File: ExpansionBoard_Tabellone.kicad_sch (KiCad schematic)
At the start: 20 parts, among them J101 RELAY, J102 UART, J103 I2C, J104 Conn_01x15, J105 Conn_01x15, J106 5V, J107 GND, J108 3V3, J109 GPIO, J110 LED, J111 RESET, J112 I2C, J113 RTC, J114 I2C

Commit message: Modificato footprint TabelloneBoard
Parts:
- U102: footprint MCU_Espressif_Footprints:ESP_WROOM_32_DevKit_HandSoldering -> PersonalLibrary:TabelloneBoard_HandSoldering
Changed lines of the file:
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@@
       (effects (font (size 1.27 1.27)))
     )
-    (property "Footprint" "MCU_Espressif_Footprints:ESP_WROOM_32_DevKit_HandSoldering" (at 105.41 27.94 0)
+    (property "Footprint" "PersonalLibrary:TabelloneBoard_HandSoldering" (at 105.41 27.94 0)
       (effects (font (size 1.27 1.27)) hide)
     )
@@
       (effects (font (size 1.27 1.27)))
     )
-    (property "Footprint" "MCU_Espressif_Footprints:ESP_WROOM_32_DevKit_HandSoldering" (at 31.75 27.94 0)
+    (property "Footprint" "PersonalLibrary:TabelloneBoard_HandSoldering" (at 31.75 27.94 0)
       (effects (font (size 1.27 1.27)) hide)
     )

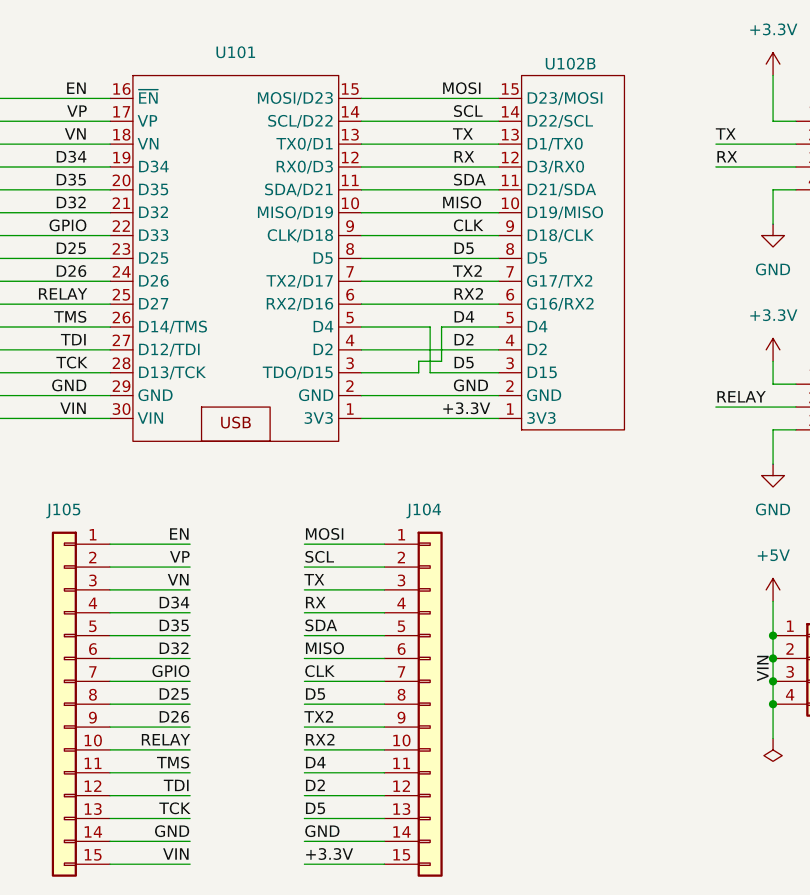
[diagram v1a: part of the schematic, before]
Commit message: Spostate le label lato Pin ESP e non lato board
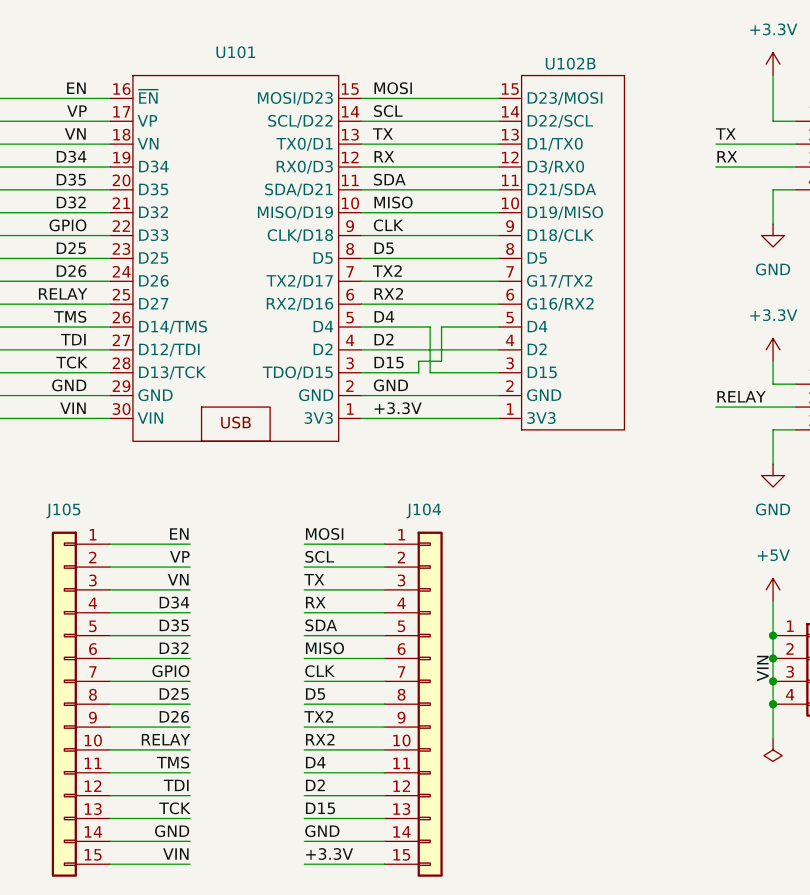
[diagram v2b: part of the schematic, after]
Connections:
- net D4: now also U101.5 (D4), U102.3 (D15); no longer U101.3 (TDO/D15), U102.5 (D4)
- net D5: no longer J104.13 (Pin_13), U101.5 (D4), U102.3 (D15)
- new net D15: J104.13 (Pin_13), U101.3 (TDO/D15), U102.5 (D4)

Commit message: Cambiate le impronte ai connettori
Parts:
- J101: footprint Connector_PinSocket_2.54mm:PinSocket_1x03_P2.54mm_Vertical -> Connector_Header_P2.54_my:PinSocket_1x03_P2.54mm_Vertical_HandSoldering
- J102, J103, J106, J107, J108, J112, J113, J114: footprint Connector_PinSocket_2.54mm:PinSocket_1x04_P2.54mm_Vertical -> Connector_Header_P2.54_my:PinSocket_1x04_P2.54mm_Vertical_HandSoldering
- J104, J105: footprint Connector_PinSocket_2.54mm:PinSocket_1x15_P2.54mm_Vertical -> Connector_Header_P2.54_my:PinSocket_1x15_P2.54mm_Vertical_HandSoldering
- J109: footprint (none) -> Connector_Header_P2.54_my:PinSocket_1x03_P2.54mm_Vertical_HandSoldering
- J110, J111: footprint (none) -> Connector_Header_P2.54_my:PinSocket_1x02_P2.54mm_Vertical_HandSoldering
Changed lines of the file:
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@@
       (effects (font (size 1.27 1.27)) (justify left))
     )
-    (property "Footprint" "Connector_PinSocket_2.54mm:PinSocket_1x04_P2.54mm_Vertical" (at 167.64 92.71 0)
+    (property "Footprint" "Connector_Header_P2.54_my:PinSocket_1x04_P2.54mm_Vertical_HandSoldering" (at 167.64 92.71 0)
       (effects (font (size 1.27 1.27)) hide)
     )
@@
       (effects (font (size 1.27 1.27)) (justify left) hide)
     )
-    (property "Footprint" "Connector_PinSocket_2.54mm:PinSocket_1x15_P2.54mm_Vertical" (at 93.98 97.79 0)
+    (property "Footprint" "Connector_Header_P2.54_my:PinSocket_1x15_P2.54mm_Vertical_HandSoldering" (at 93.98 97.79 0)
       (effects (font (size 1.27 1.27)) hide)
     )
@@
       (effects (font (size 1.27 1.27)) (justify left))
     )
-    (property "Footprint" "Connector_PinSocket_2.54mm:PinSocket_1x03_P2.54mm_Vertical" (at 139.7 64.77 0)
+    (property "Footprint" "Connector_Header_P2.54_my:PinSocket_1x03_P2.54mm_Vertical_HandSoldering" (at 139.7 64.77 0)
       (effects (font (size 1.27 1.27)) hide)
     )
@@
       (effects (font (size 1.27 1.27)) (justify left))
     )
-    (property "Footprint" "Connector_PinSocket_2.54mm:PinSocket_1x04_P2.54mm_Vertical" (at 237.49 92.71 0)
+    (property "Footprint" "Connector_Header_P2.54_my:PinSocket_1x04_P2.54mm_Vertical_HandSoldering" (at 237.49 92.71 0)
       (effects (font (size 1.27 1.27)) hide)
     )
@@
       (effects (font (size 1.27 1.27)) (justify left))
     )
-    (property "Footprint" "" (at 165.1 64.77 0)
+    (property "Footprint" "Connector_Header_P2.54_my:PinSocket_1x03_P2.54mm_Vertical_HandSoldering" (at 165.1 64.77 0)
       (effects (font (size 1.27 1.27)) hide)
     )
@@
       (effects (font (size 1.27 1.27)) (justify left))
     )
-    (property "Footprint" "Connector_PinSocket_2.54mm:PinSocket_1x04_P2.54mm_Vertical" (at 201.93 64.77 0)
+    (property "Footprint" "Connector_Header_P2.54_my:PinSocket_1x04_P2.54mm_Vertical_HandSoldering" (at 201.93 64.77 0)
       (effects (font (size 1.27 1.27)) hide)
     )
@@
       (effects (font (size 1.27 1.27)) (justify left))
     )
-    (property "Footprint" "" (at 201.93 34.29 0)
+    (property "Footprint" "Connector_Header_P2.54_my:PinSocket_1x02_P2.54mm_Vertical_HandSoldering" (at 201.93 34.29 0)
       (effects (font (size 1.27 1.27)) hide)
     )
@@
       (effects (font (size 1.27 1.27)) (justify left))
     )
-    (property "Footprint" "Connector_PinSocket_2.54mm:PinSocket_1x04_P2.54mm_Vertical" (at 139.7 35.56 0)
+    (property "Footprint" "Connector_Header_P2.54_my:PinSocket_1x04_P2.54mm_Vertical_HandSoldering" (at 139.7 35.56 0)
       (effects (font (size 1.27 1.27)) hide)
     )
@@
       (effects (font (size 1.27 1.27)) (justify left))
     )
-    (property "Footprint" "Connector_PinSocket_2.54mm:PinSocket_1x04_P2.54mm_Vertical" (at 152.4 92.71 0)
+    (property "Footprint" "Connector_Header_P2.54_my:PinSocket_1x04_P2.54mm_Vertical_HandSoldering" (at 152.4 92.71 0)
       (effects (font (size 1.27 1.27)) hide)
     )
@@
       (effects (font (size 1.27 1.27)) (justify left))
     )
-    (property "Footprint" "" (at 240.03 34.29 0)
+    (property "Footprint" "Connector_Header_P2.54_my:PinSocket_1x02_P2.54mm_Vertical_HandSoldering" (at 240.03 34.29 0)
       (effects (font (size 1.27 1.27)) hide)
     )
@@
       (effects (font (size 1.27 1.27)) hide)
     )
-    (property "Footprint" "Connector_PinSocket_2.54mm:PinSocket_1x15_P2.54mm_Vertical" (at 53.34 97.79 0)
+    (property "Footprint" "Connector_Header_P2.54_my:PinSocket_1x15_P2.54mm_Vertical_HandSoldering" (at 53.34 97.79 0)
       (effects (font (size 1.27 1.27)) hide)
     )
@@
       (effects (font (size 1.27 1.27)) (justify left))
     )
-    (property "Footprint" "Connector_PinSocket_2.54mm:PinSocket_1x04_P2.54mm_Vertical" (at 237.49 64.77 0)
+    (property "Footprint" "Connector_Header_P2.54_my:PinSocket_1x04_P2.54mm_Vertical_HandSoldering" (at 237.49 64.77 0)
       (effects (font (size 1.27 1.27)) hide)
     )
@@
       (effects (font (size 1.27 1.27)) (justify left))
     )
-    (property "Footprint" "Connector_PinSocket_2.54mm:PinSocket_1x04_P2.54mm_Vertical" (at 137.16 92.71 0)
+    (property "Footprint" "Connector_Header_P2.54_my:PinSocket_1x04_P2.54mm_Vertical_HandSoldering" (at 137.16 92.71 0)
       (effects (font (size 1.27 1.27)) hide)
     )
@@
       (effects (font (size 1.27 1.27)) (justify left))
     )
-    (property "Footprint" "Connector_PinSocket_2.54mm:PinSocket_1x04_P2.54mm_Vertical" (at 201.93 92.71 0)
-      (effects (font (size 1.27 1.27)) hide)
-    )
+    (property "Footprint" "Connector_Header_P2.54_my:PinSocket_1x04_P2.54mm_Vertical_HandSoldering" (at 201.93 92.71 0)
+      (effects (font (size 1.27 1.27)) hide)
+    )

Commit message: Cambiato un footprint
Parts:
- R101: footprint Resistor_THT:R_Axial_DIN0309_L9.0mm_D3.2mm_P15.24mm_Horizontal -> Resistor_THT:R_Axial_DIN0309_L9.0mm_D3.2mm_P12.70mm_Horizontal
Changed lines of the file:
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@@
       (effects (font (size 1.27 1.27)))
     )
-    (property "Footprint" "Resistor_THT:R_Axial_DIN0309_L9.0mm_D3.2mm_P15.24mm_Horizontal" (at 187.96 32.512 90)
+    (property "Footprint" "Resistor_THT:R_Axial_DIN0309_L9.0mm_D3.2mm_P12.70mm_Horizontal" (at 187.96 32.512 90)
       (effects (font (size 1.27 1.27)) hide)
     )

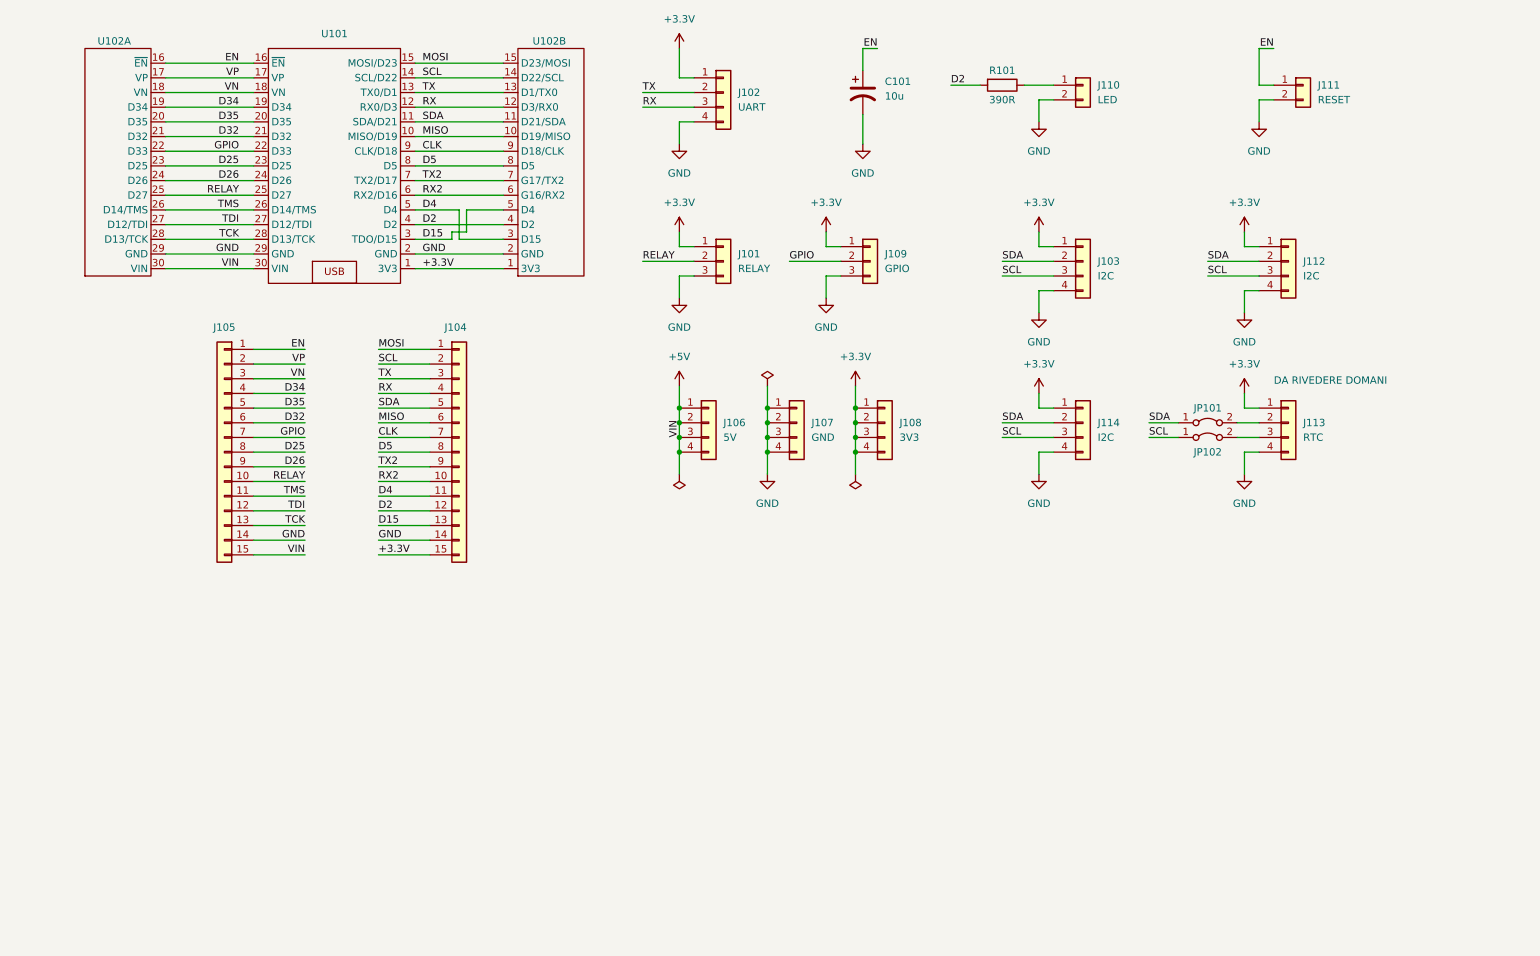
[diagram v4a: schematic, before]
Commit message: Aggiunti i Relè nello schematico
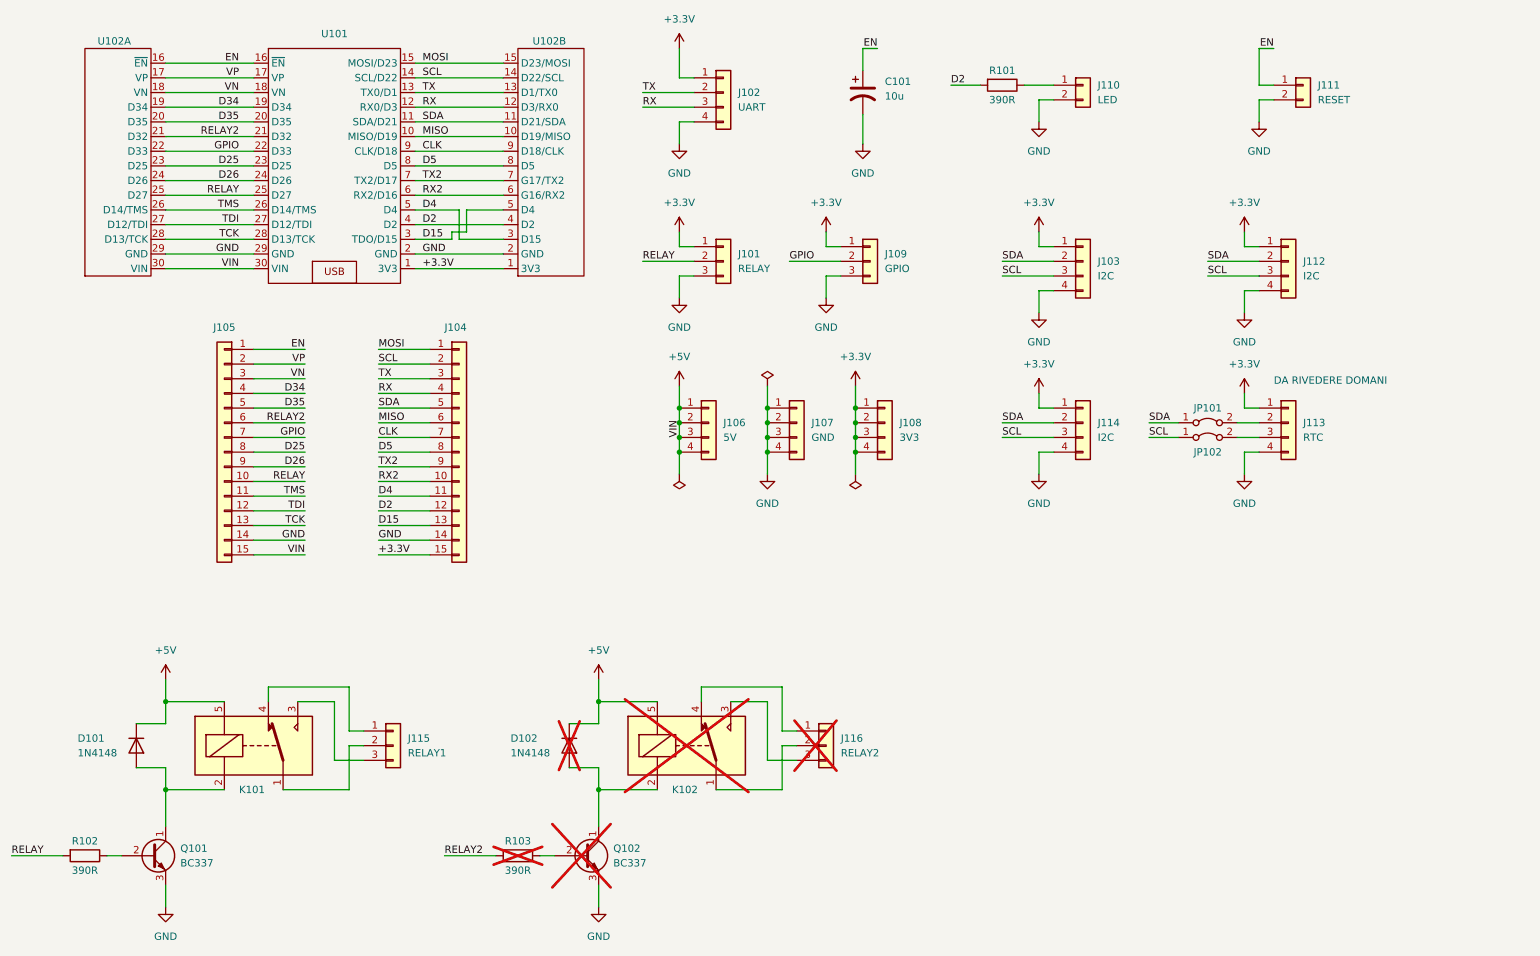
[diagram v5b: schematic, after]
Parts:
- added D101, D102: 1N4148, Diode_THT:D_DO-35_SOD27_P7.62mm_Horizontal, symbol Diode:1N4148
- added J115: RELAY1, Connector_Header_P2.54_my:PinSocket_1x03_P2.54mm_Vertical_HandSoldering, symbol Connector_Generic:Conn_01x03
- added J116: RELAY2, Connector_Header_P2.54_my:PinSocket_1x03_P2.54mm_Vertical_HandSoldering, symbol Connector_Generic:Conn_01x03
- added K101, K102: SANYOU_SRD_Form_C, Relay_THT:Relay_SPDT_SANYOU_SRD_Series_Form_C, symbol Relay:SANYOU_SRD_Form_C
- added Q101, Q102: BC337, Package_TO_SOT_THT:TO-92_HandSolder, symbol Transistor_BJT:BC337
- added R102, R103: 390R, Resistor_THT:R_Axial_DIN0207_L6.3mm_D2.5mm_P10.16mm_Horizontal, symbol Device:R
- R101: footprint Resistor_THT:R_Axial_DIN0309_L9.0mm_D3.2mm_P12.70mm_Horizontal -> Resistor_THT:R_Axial_DIN0207_L6.3mm_D2.5mm_P10.16mm_Horizontal
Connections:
- net +5V: now also D101.1 (K), D102.1 (K), K101.5, K102.5
- net GND: now also Q101.3 (E), Q102.3 (E)
- net RELAY: now also R102.2
- net D32 renamed RELAY2
- net RELAY2: now also R103.2
- new net: D102.2 (A), K102.2, Q102.1 (C)
- new net: Q102.2 (B), R103.1
- new net: Q101.2 (B), R102.1
- new net: J116.2 (Pin_2), K102.1
- new net: J116.3 (Pin_3), K102.3
- new net: J116.1 (Pin_1), K102.4
- new net: D101.2 (A), K101.2, Q101.1 (C)
- new net: J115.2 (Pin_2), K101.1
- new net: J115.3 (Pin_3), K101.3
- new net: J115.1 (Pin_1), K101.4

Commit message: Modificato connettore RTC
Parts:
- removed J103, J112, J114: I2C, Connector_Header_P2.54_my:PinSocket_1x04_P2.54mm_Vertical_HandSoldering, symbol Connector_Generic:Conn_01x04
- removed J113: RTC, Connector_Header_P2.54_my:PinSocket_1x04_P2.54mm_Vertical_HandSoldering, symbol Connector_Generic:Conn_01x04
- added J106, J107, J111, J117: GPIO, Connector_Header_P2.54_my:PinSocket_1x03_P2.54mm_Vertical_HandSoldering, symbol Connector_Generic:Conn_01x03
- added J112: RTC, Connector_Header_P2.54_my:PinSocket_1x06_P2.54mm_Vertical_HandSoldering, symbol Connector_Generic:Conn_01x06
- renumbered J110 to J101, J111 to J102, J102 to J103, J101 to J104, J109 to J105, J106 to J108, J107 to J109, J108 to J110, J105 to J113, J104 to J114, U102 to U101, U101 to U102
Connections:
- net +3.3V: now also J111.1 (Pin_1), J111.2 (Pin_2), J111.3 (Pin_3), J112.2 (Pin_2)
- net GND: now also J112.1 (Pin_1), J117.1 (Pin_1), J117.2 (Pin_2), J117.3 (Pin_3)
- net SCL: now also J107.1 (Pin_1), J107.2 (Pin_2), J107.3 (Pin_3)
- net SDA: now also J106.1 (Pin_1), J106.2 (Pin_2), J106.3 (Pin_3)
- net at JP101.2 (B): now also J112.3 (Pin_3)
- net at JP102.2 (B): now also J112.4 (Pin_4)
- no-connect marks 0 -> 2
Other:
- note removed: "DA RIVEDERE DOMANI"
